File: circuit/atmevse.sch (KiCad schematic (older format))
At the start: 24 parts

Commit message: Continue schematic capture
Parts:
- removed ?: VTX-214-005-112, symbol smartevse:VTX-214-005-112
- removed C? (x8): 10u16V, symbol Device:C_Small
- removed C? (x3): 100n, symbol Device:C_Small
- removed D?: PMEG4010CEH, Diode_SMD:D_SOD-128, symbol Diode:PMEG4050EP
- removed IC?: TL7660, symbol smartevse:TL7660
- removed K? (x3): AQH213A, symbol smartevse:AQH213A
- removed L?: 2.2uH, symbol Device:L
- removed R?: 10K, symbol Device:R_Small
- removed R?: 31.6K, symbol Device:R_Small
- removed RV? (x3): Varistor, symbol Device:Varistor
- removed U?: AOZ1280CI, Package_TO_SOT_SMD:SOT-23-6, symbol Regulator_Switching:AOZ1280CI
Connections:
- no-connect marks 5 -> 0
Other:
- note added: "ATmega4808\nRS485 Transceiver\nLock Actuator\nTemperature Sensor"
- note added: "Mains Input Connector \nContactor Relays\n12V Power Supply\n3.3V DC Converter\n-12V Voltage Inverter"
- note removed: "12V Inverter\n"
- note removed: "12V Power Supply"
- note removed: "3.3V Regulator"
- note removed: "Mains Input & Contactor Output\n"
- note removed: "Solid State Relays"

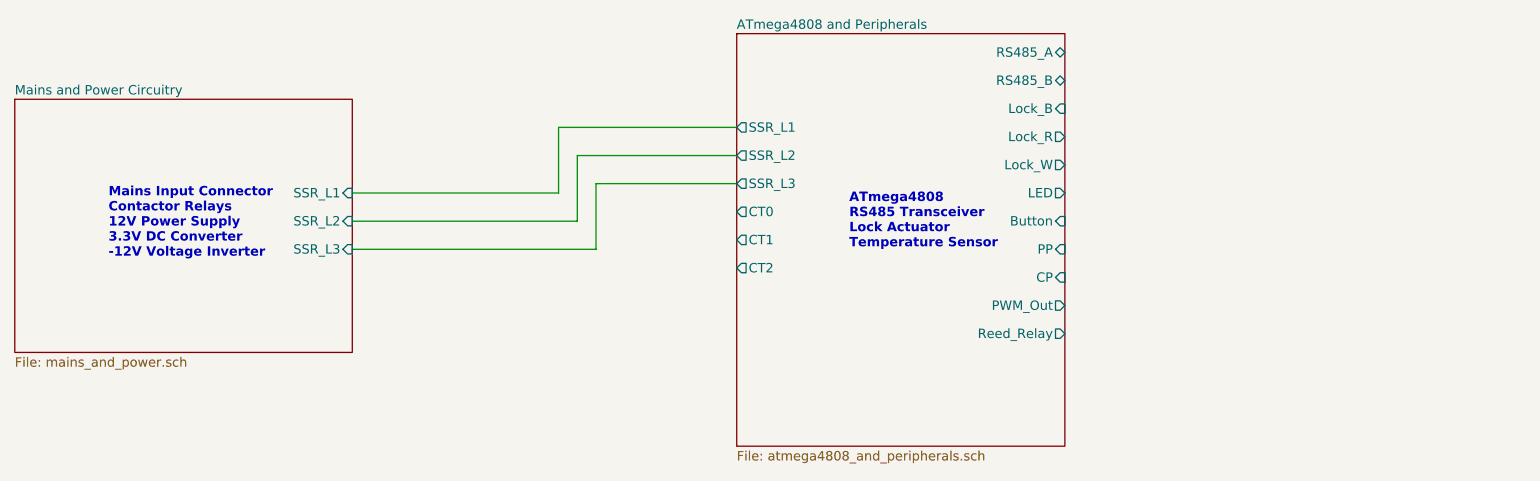
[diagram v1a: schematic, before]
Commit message: Update to rev0.1 of atmevse circuit
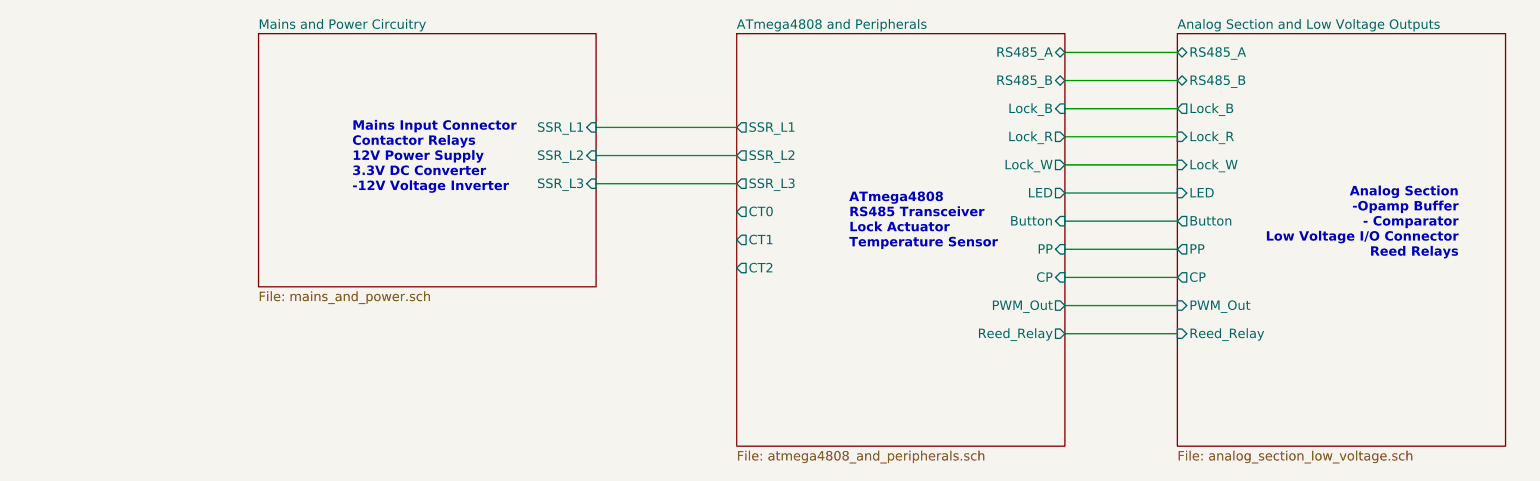
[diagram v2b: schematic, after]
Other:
- note added: "Analog Section\n-Opamp Buffer\n- Comparator\nLow Voltage I/O Connector\nReed Relays"
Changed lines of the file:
@@
 $Descr A4 11693 8268
 encoding utf-8
-Sheet 1 3
+Sheet 1 4
 Title "ATmega4808 EVSE"
 Date "2020-04-09"
@@
 $EndDescr
 $Sheet
-S 1000 3050 1800 1350
+S 2300 2700 1800 1350
 U 5E98FA8A
 F0 "Mains and Power Circuitry" 50
 F1 "mains_and_power.sch" 50
-F2 "SSR_L1" I R 2800 3550 50
-F3 "SSR_L2" I R 2800 3700 50
-F4 "SSR_L3" I R 2800 3850 50
+F2 "SSR_L1" I R 4100 3200 50
+F3 "SSR_L2" I R 4100 3350 50
+F4 "SSR_L3" I R 4100 3500 50
 $EndSheet
-Text Notes 1500 3900 0    50   ~ 10
+Text Notes 2800 3550 0    50   ~ 10
 Mains Input Connector \nContactor Relays\n12V Power Supply\n3.3V DC Converter\n-12V Voltage Inverter
 $Sheet
@@
 Text Notes 5450 3850 0    50   ~ 10
 ATmega4808\nRS485 Transceiver\nLock Actuator\nTemperature Sensor
+$Sheet
+S 7200 2700 1750 2200
+U 5E903BF9
+F0 "Analog Section and Low Voltage Outputs" 50
+F1 "analog_section_low_voltage.sch" 50
+F2 "PWM_Out" I L 7200 4150 50
+F3 "CP" O L 7200 4000 50
+F4 "LED" I L 7200 3550 50
+F5 "RS485_A" B L 7200 2800 50
+F6 "RS485_B" B L 7200 2950 50
+F7 "Lock_B" O L 7200 3100 50
+F8 "Lock_R" I L 7200 3250 50
+F9 "Lock_W" I L 7200 3400 50
+F10 "PP" O L 7200 3850 50
+F11 "Button" O L 7200 3700 50
+F12 "Reed_Relay" I L 7200 4300 50
+$EndSheet
 Wire Wire Line
-	2800 3550 3900 3550
+	6600 2800 7200 2800
 Wire Wire Line
-	3900 3550 3900 3200
+	7200 2950 6600 2950
 Wire Wire Line
-	3900 3200 4850 3200
+	6600 3100 7200 3100
 Wire Wire Line
-	4850 3350 4000 3350
+	7200 3250 6600 3250
 Wire Wire Line
-	4000 3350 4000 3700
+	6600 3400 7200 3400
 Wire Wire Line
-	4000 3700 2800 3700
+	6600 3550 7200 3550
 Wire Wire Line
-	2800 3850 4100 3850
+	6600 3850 7200 3850
 Wire Wire Line
-	4100 3850 4100 3500
+	6600 4000 7200 4000
 Wire Wire Line
-	4100 3500 4850 3500
+	6600 4150 7200 4150
+Wire Wire Line
+	7200 4300 6600 4300
+Wire Wire Line
+	6600 3700 7200 3700
+Text Notes 8700 3900 2    50   ~ 10
+Analog Section\n-Opamp Buffer\n- Comparator\nLow Voltage I/O Connector\nReed Relays
+Wire Wire Line
+	4850 3200 4100 3200
+Wire Wire Line
+	4850 3350 4100 3350
+Wire Wire Line
+	4850 3500 4100 3500
 $EndSCHEMATC

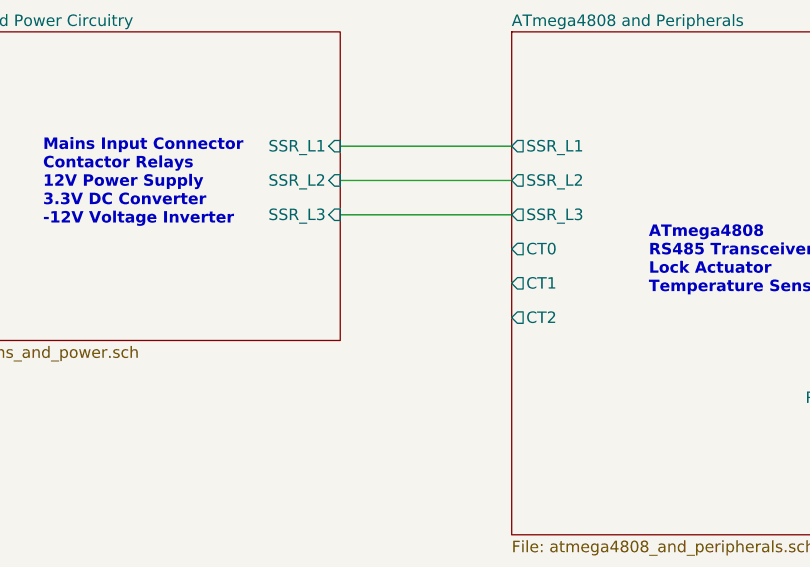
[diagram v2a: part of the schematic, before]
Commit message: Update schematic to rev0.2
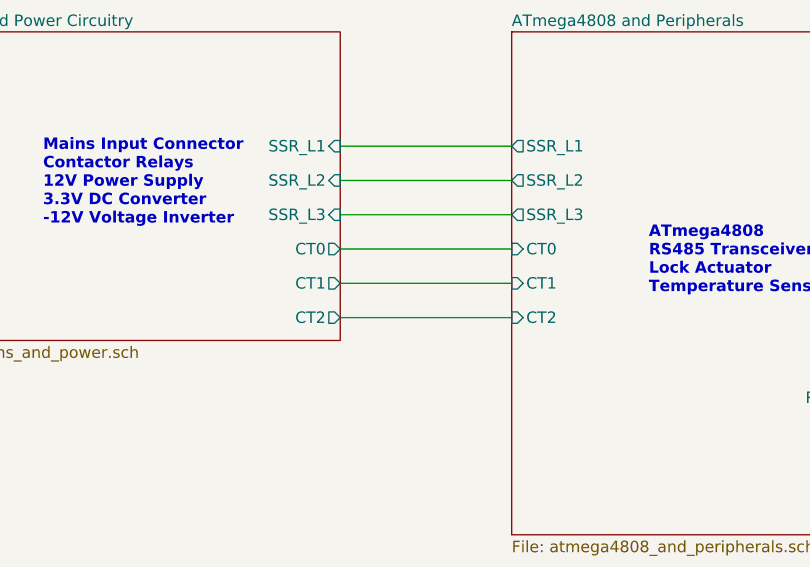
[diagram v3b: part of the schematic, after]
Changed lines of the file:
@@
 Sheet 1 4
 Title "ATmega4808 EVSE"
-Date "2020-04-09"
-Rev "0.1"
+Date "2020-04-10"
+Rev "0.2"
 Comp ""
 Comment1 ""
@@
 F3 "SSR_L2" I R 4100 3350 50
 F4 "SSR_L3" I R 4100 3500 50
+F5 "CT0" O R 4100 3650 50
+F6 "CT1" O R 4100 3800 50
+F7 "CT2" O R 4100 3950 50
 $EndSheet
 Text Notes 2800 3550 0    50   ~ 10
@@
 F9 "Lock_B" I R 6600 3100 50
 F10 "LED" O R 6600 3550 50
-F11 "CT0" O L 4850 3650 50
-F12 "CT1" O L 4850 3800 50
-F13 "CT2" O L 4850 3950 50
+F11 "CT0" I L 4850 3650 50
+F12 "CT1" I L 4850 3800 50
+F13 "CT2" I L 4850 3950 50
 F14 "Button" I R 6600 3700 50
 F15 "PP" I R 6600 3850 50
@@
 Wire Wire Line
 	4850 3500 4100 3500
+Wire Wire Line
+	4100 3650 4850 3650
+Wire Wire Line
+	4100 3800 4850 3800
+Wire Wire Line
+	4100 3950 4850 3950
 $EndSCHEMATC

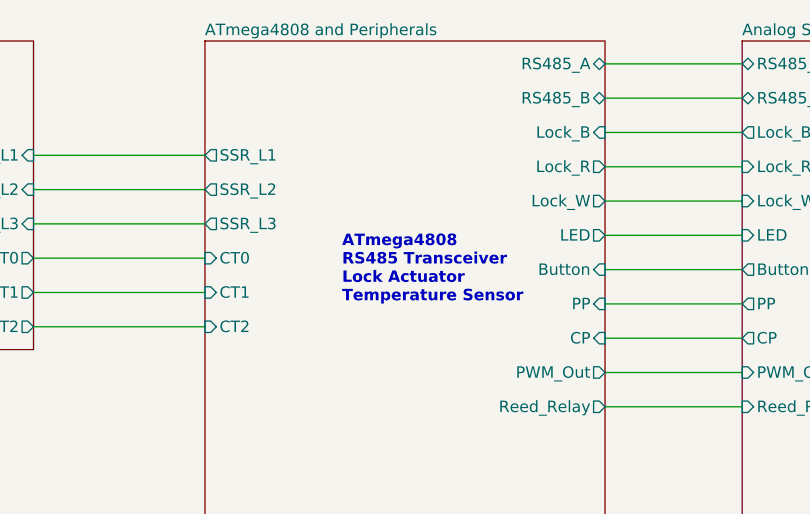
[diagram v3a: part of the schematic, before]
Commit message: Update schematic with suggestions
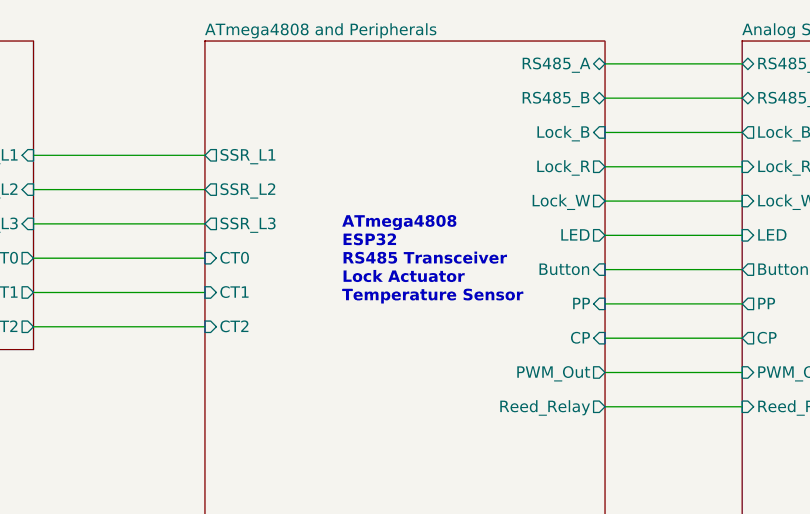
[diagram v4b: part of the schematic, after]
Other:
- note added: "ATmega4808\nESP32\nRS485 Transceiver\nLock Actuator\nTemperature Sensor"
- note removed: "ATmega4808\nRS485 Transceiver\nLock Actuator\nTemperature Sensor"
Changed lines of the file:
@@
 Sheet 1 4
 Title "ATmega4808 EVSE"
-Date "2020-04-10"
-Rev "0.2"
+Date "2020-05-13"
+Rev "0.4"
 Comp ""
 Comment1 ""
@@
 $EndSheet
 Text Notes 5450 3850 0    50   ~ 10
-ATmega4808\nRS485 Transceiver\nLock Actuator\nTemperature Sensor
+ATmega4808\nESP32\nRS485 Transceiver\nLock Actuator\nTemperature Sensor
 $Sheet
 S 7200 2700 1750 2200

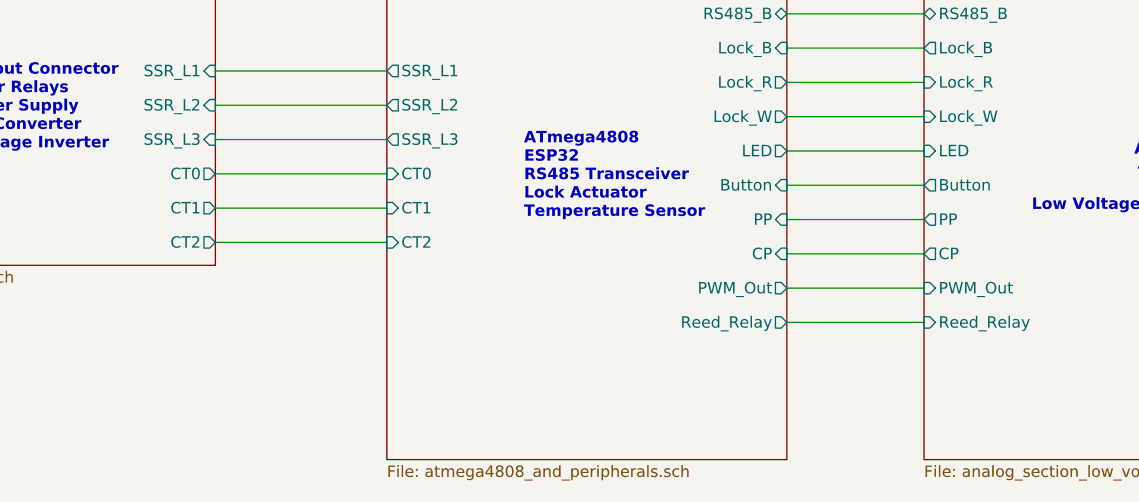
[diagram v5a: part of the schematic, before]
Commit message: Edit schematic to rev0.6
Updated schematic with ESP32, CT inputs moved, Button input circuit new.
Temp sens removed, will use internal sensor in ATmega4808
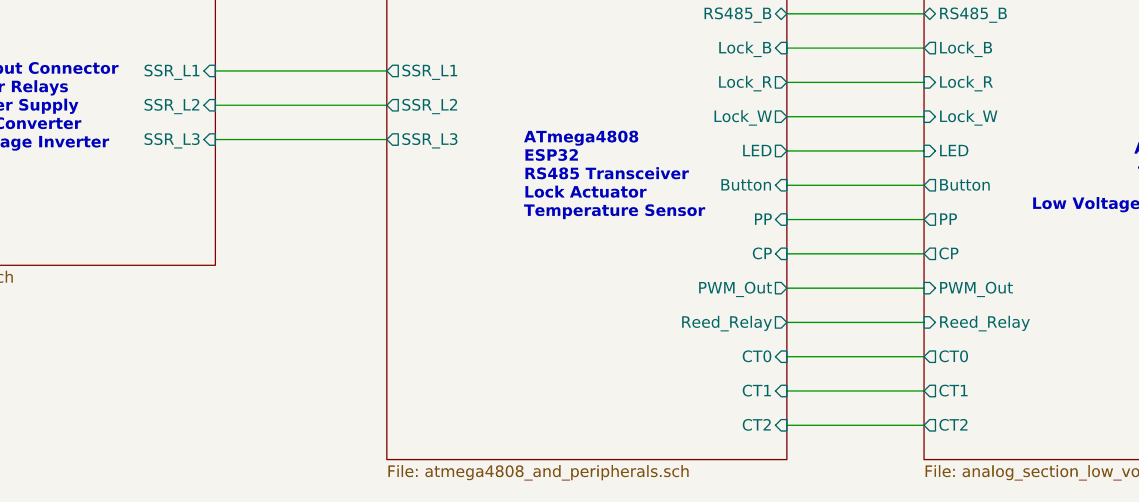
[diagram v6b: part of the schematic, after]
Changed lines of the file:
@@
 Title "ATmega4808 EVSE"
 Date "2020-05-14"
-Rev "0.5"
+Rev "0.6"
 Comp ""
 Comment1 "TODO: finish button/LED connections"
 Comment2 "TODO: remove TempSensor, free Pin"
 Comment3 "TODO: third ATmega UART"
-Comment4 ""
+Comment4 "DONE: Switch CT inputs to J2"
 $EndDescr
 $Sheet
@@
 F3 "SSR_L2" I R 4100 3350 50
 F4 "SSR_L3" I R 4100 3500 50
-F5 "CT0" O R 4100 3650 50
-F6 "CT1" O R 4100 3800 50
-F7 "CT2" O R 4100 3950 50
 $EndSheet
 Text Notes 2800 3550 0    50   ~ 10
@@
 F9 "Lock_B" I R 6600 3100 50
 F10 "LED" O R 6600 3550 50
-F11 "CT0" I L 4850 3650 50
-F12 "CT1" I L 4850 3800 50
-F13 "CT2" I L 4850 3950 50
+F11 "CT0" I R 6600 4450 50
+F12 "CT1" I R 6600 4600 50
+F13 "CT2" I R 6600 4750 50
 F14 "Button" I R 6600 3700 50
 F15 "PP" I R 6600 3850 50
@@
 F11 "Button" O L 7200 3700 50
 F12 "Reed_Relay" I L 7200 4300 50
+F13 "CT0" O L 7200 4450 50
+F14 "CT1" O L 7200 4600 50
+F15 "CT2" O L 7200 4750 50
 $EndSheet
 Wire Wire Line
@@
 	4850 3500 4100 3500
 Wire Wire Line
-	4100 3650 4850 3650
+	6600 4450 7200 4450
 Wire Wire Line
-	4100 3800 4850 3800
+	6600 4600 7200 4600
 Wire Wire Line
-	4100 3950 4850 3950
+	6600 4750 7200 4750
 $EndSCHEMATC

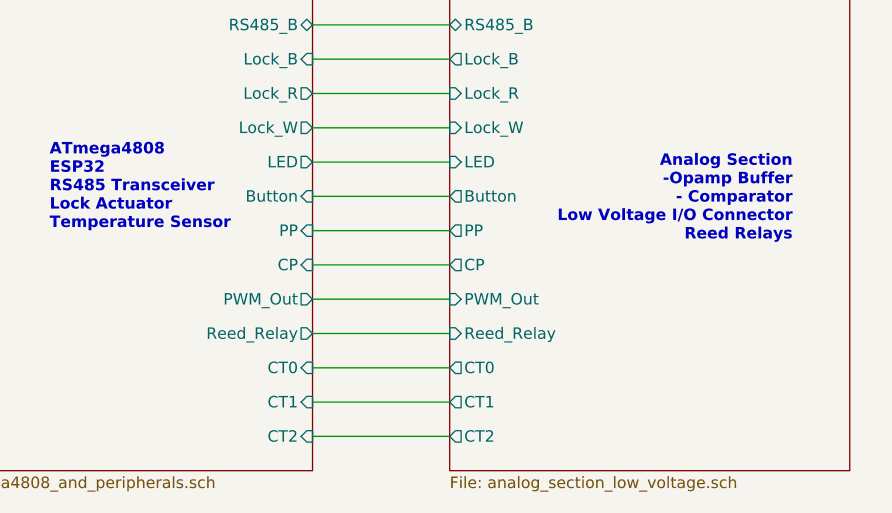
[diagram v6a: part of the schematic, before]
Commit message: Update Parts List with Mouser ordering info
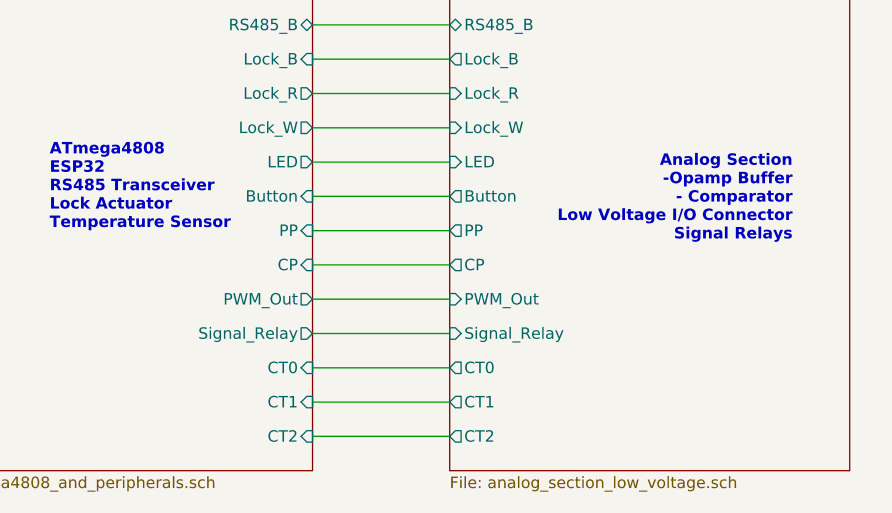
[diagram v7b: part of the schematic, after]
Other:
- note added: "Analog Section\n-Opamp Buffer\n- Comparator\nLow Voltage I/O Connector\nSignal Relays"
- note removed: "Analog Section\n-Opamp Buffer\n- Comparator\nLow Voltage I/O Connector\nReed Relays"
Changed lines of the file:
@@
 Sheet 1 4
 Title "ATmega4808 EVSE"
-Date "2020-05-14"
-Rev "0.6"
+Date "2020-05-29"
+Rev "0.7"
 Comp ""
 Comment1 "TODO: finish button/LED connections"
-Comment2 "TODO: remove TempSensor, free Pin"
-Comment3 "TODO: third ATmega UART"
-Comment4 "DONE: Switch CT inputs to J2"
+Comment2 ""
+Comment3 ""
+Comment4 ""
 $EndDescr
 $Sheet
@@
 F16 "CP" I R 6600 4000 50
 F17 "PWM_Out" O R 6600 4150 50
-F18 "Reed_Relay" O R 6600 4300 50
+F18 "Signal_Relay" O R 6600 4300 50
 $EndSheet
 Text Notes 5450 3850 0    50   ~ 10
@@
 F10 "PP" O L 7200 3850 50
 F11 "Button" O L 7200 3700 50
-F12 "Reed_Relay" I L 7200 4300 50
-F13 "CT0" O L 7200 4450 50
-F14 "CT1" O L 7200 4600 50
-F15 "CT2" O L 7200 4750 50
+F12 "CT0" O L 7200 4450 50
+F13 "CT1" O L 7200 4600 50
+F14 "CT2" O L 7200 4750 50
+F15 "Signal_Relay" I L 7200 4300 50
 $EndSheet
 Wire Wire Line
@@
 	6600 3700 7200 3700
 Text Notes 8700 3900 2    50   ~ 10
-Analog Section\n-Opamp Buffer\n- Comparator\nLow Voltage I/O Connector\nReed Relays
+Analog Section\n-Opamp Buffer\n- Comparator\nLow Voltage I/O Connector\nSignal Relays
 Wire Wire Line
 	4850 3200 4100 3200

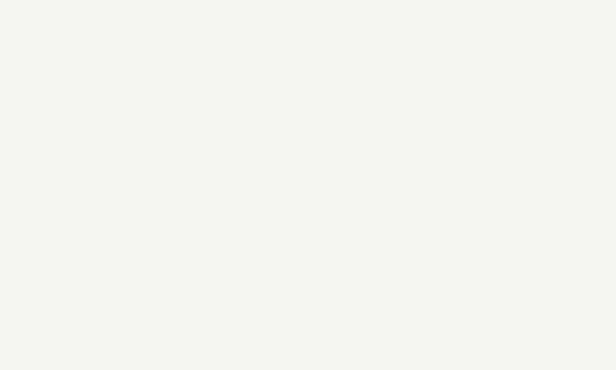
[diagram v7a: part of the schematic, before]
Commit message: Finish schematic rev1 and footprint assignment
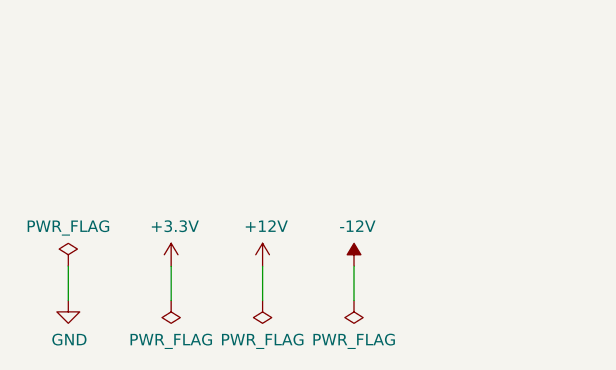
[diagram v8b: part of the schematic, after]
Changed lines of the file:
@@
 Sheet 1 4
 Title "ATmega4808 EVSE"
-Date "2020-05-29"
-Rev "0.7"
+Date "2020-06-01"
+Rev "1.0"
 Comp ""
 Comment1 "TODO: finish button/LED connections"
@@
 Wire Wire Line
 	6600 4750 7200 4750
+$Comp
+L power:+3.3V #PWR0110
+U 1 1 5ED97DE8
+P 1500 6000
+F 0 "#PWR0110" H 1500 5850 50  0001 C CNN
+F 1 "+3.3V" H 1515 6173 50  0000 C CNN
+F 2 "" H 1500 6000 50  0001 C CNN
+F 3 "" H 1500 6000 50  0001 C CNN
+	1    1500 6000
+	1    0    0    -1
+$EndComp
+$Comp
+L power:GND #PWR0111
+U 1 1 5ED983F4
+P 1050 6150
+F 0 "#PWR0111" H 1050 5900 50  0001 C CNN
+F 1 "GND" H 1055 5977 50  0000 C CNN
+F 2 "" H 1050 6150 50  0001 C CNN
+F 3 "" H 1050 6150 50  0001 C CNN
+	1    1050 6150
+	1    0    0    -1
+$EndComp
+$Comp
+L power:+12V #PWR0112
+U 1 1 5ED9882E
+P 1900 6000
+F 0 "#PWR0112" H 1900 5850 50  0001 C CNN
+F 1 "+12V" H 1915 6173 50  0000 C CNN
+F 2 "" H 1900 6000 50  0001 C CNN
+F 3 "" H 1900 6000 50  0001 C CNN
+	1    1900 6000
+	1    0    0    -1
+$EndComp
+$Comp
+L power:-12V #PWR0113
+U 1 1 5ED9957C
+P 2300 6000
+F 0 "#PWR0113" H 2300 6100 50  0001 C CNN
+F 1 "-12V" H 2315 6173 50  0000 C CNN
+F 2 "" H 2300 6000 50  0001 C CNN
+F 3 "" H 2300 6000 50  0001 C CNN
+	1    2300 6000
+	1    0    0    -1
+$EndComp
+$Comp
+L power:PWR_FLAG #FLG0101
+U 1 1 5ED996AE
+P 1500 6150
+F 0 "#FLG0101" H 1500 6225 50  0001 C CNN
+F 1 "PWR_FLAG" H 1500 6323 50  0000 C CNN
+F 2 "" H 1500 6150 50  0001 C CNN
+F 3 "~" H 1500 6150 50  0001 C CNN
+	1    1500 6150
+	-1   0    0    1
+$EndComp
+$Comp
+L power:PWR_FLAG #FLG0102
+U 1 1 5ED99E56
+P 2300 6150
+F 0 "#FLG0102" H 2300 6225 50  0001 C CNN
+F 1 "PWR_FLAG" H 2300 6323 50  0000 C CNN
+F 2 "" H 2300 6150 50  0001 C CNN
+F 3 "~" H 2300 6150 50  0001 C CNN
+	1    2300 6150
+	-1   0    0    1
+$EndComp
+$Comp
+L power:PWR_FLAG #FLG0103
+U 1 1 5ED9AF19
+P 1900 6150
+F 0 "#FLG0103" H 1900 6225 50  0001 C CNN
+F 1 "PWR_FLAG" H 1900 6323 50  0000 C CNN
+F 2 "" H 1900 6150 50  0001 C CNN
+F 3 "~" H 1900 6150 50  0001 C CNN
+	1    1900 6150
+	-1   0    0    1
+$EndComp
+$Comp
+L power:PWR_FLAG #FLG0104
+U 1 1 5ED9B7C1
+P 1050 6000
+F 0 "#FLG0104" H 1050 6075 50  0001 C CNN
+F 1 "PWR_FLAG" H 1050 6173 50  0000 C CNN
+F 2 "" H 1050 6000 50  0001 C CNN
+F 3 "~" H 1050 6000 50  0001 C CNN
+	1    1050 6000
+	1    0    0    -1
+$EndComp
+Wire Wire Line
+	1050 6000 1050 6150
+Wire Wire Line
+	1500 6000 1500 6150
+Wire Wire Line
+	1900 6000 1900 6150
+Wire Wire Line
+	2300 6000 2300 6150
 $EndSCHEMATC
